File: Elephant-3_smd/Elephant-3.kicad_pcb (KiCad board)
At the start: 2 copper layers, 90.2 x 58.4 mm, 61 parts, among them CON1 ISP, J1 7-25V, J10 Micro_SD_Card, J11 IgnCap, J12 Main, J2 ADC2, J3 ADC1, J4 ADC0, J5 Switch, J6 18V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

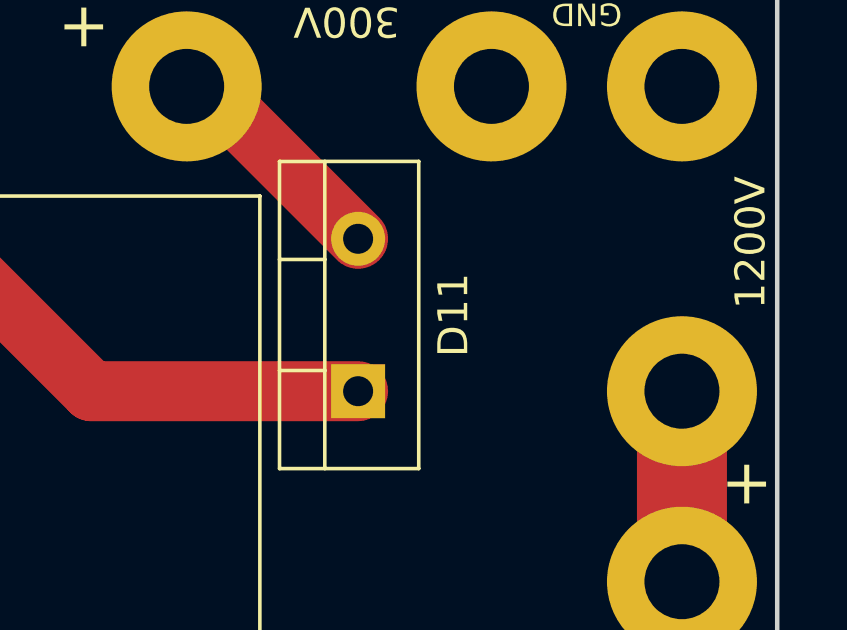
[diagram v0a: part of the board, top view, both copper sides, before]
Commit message: Added project files for smd version and replaced some component to generic
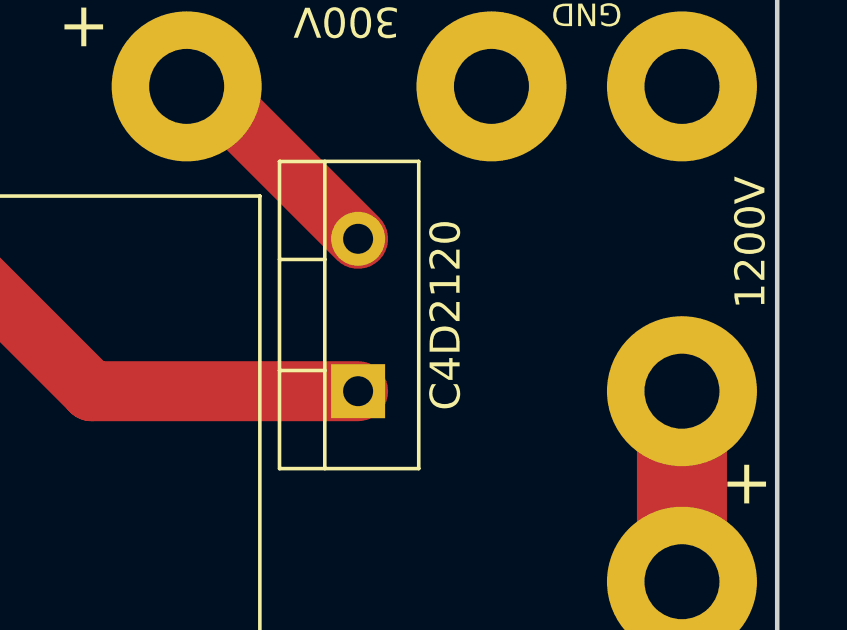
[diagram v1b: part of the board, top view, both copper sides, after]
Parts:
- D11: value D -> C4D2120
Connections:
- J10 pad 1: (no net) -> Net-(J10-Pad1)
- J10 pad 10: (no net) -> Net-(J10-Pad10)
- J10 pad 8: (no net) -> Net-(J10-Pad8)
- J10 pad 9: (no net) -> Net-(J10-Pad9)
- U2 pad 12: (no net) -> Net-(U2-Pad12)
- U2 pad 14: (no net) -> Net-(U2-Pad14)
- U2 pad 15: (no net) -> Net-(U2-Pad15)
- U2 pad 2: (no net) -> Net-(U2-Pad2)
- U2 pad 21: (no net) -> Net-(U2-Pad21)
- U2 pad 26: (no net) -> Net-(U2-Pad26)
- U2 pad 27: (no net) -> Net-(U2-Pad27)
- U2 pad 3: (no net) -> Net-(U2-Pad3)
- U2 pad 5: (no net) -> Net-(U2-Pad5)
- U2 pad 6: (no net) -> Net-(U2-Pad6)
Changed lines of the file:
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@@
     (zones 0)
     (modules 61)
-    (nets 35)
+    (nets 49)
   )
   (page A4)
@@
   (net 33 "Net-(C11-Pad1)")
   (net 34 "Net-(C13-Pad2)")
+  (net 35 "Net-(J10-Pad9)")
+  (net 36 "Net-(J10-Pad8)")
+  (net 37 "Net-(J10-Pad1)")
+  (net 38 "Net-(J10-Pad10)")
+  (net 39 "Net-(U2-Pad15)")
+  (net 40 "Net-(U2-Pad2)")
+  (net 41 "Net-(U2-Pad3)")
+  (net 42 "Net-(U2-Pad5)")
+  (net 43 "Net-(U2-Pad6)")
+  (net 44 "Net-(U2-Pad21)")
+  (net 45 "Net-(U2-Pad12)")
+  (net 46 "Net-(U2-Pad26)")
+  (net 47 "Net-(U2-Pad27)")
+  (net 48 "Net-(U2-Pad14)")
   (net_class Default "This is the default net class."
     (clearance 0.2)
@@
     (add_net "Net-(D4-Pad1)")
     (add_net "Net-(D6-Pad1)")
+    (add_net "Net-(J10-Pad1)")
+    (add_net "Net-(J10-Pad10)")
     (add_net "Net-(J10-Pad2)")
     (add_net "Net-(J10-Pad3)")
     (add_net "Net-(J10-Pad5)")
+    (add_net "Net-(J10-Pad8)")
+    (add_net "Net-(J10-Pad9)")
     (add_net "Net-(J5-Pad1)")
     (add_net "Net-(Q1-Pad1)")
     (add_net "Net-(Q2-Pad1)")
     (add_net "Net-(U2-Pad11)")
+    (add_net "Net-(U2-Pad12)")
     (add_net "Net-(U2-Pad13)")
+    (add_net "Net-(U2-Pad14)")
+    (add_net "Net-(U2-Pad15)")
     (add_net "Net-(U2-Pad16)")
+    (add_net "Net-(U2-Pad2)")
+    (add_net "Net-(U2-Pad21)")
+    (add_net "Net-(U2-Pad26)")
+    (add_net "Net-(U2-Pad27)")
+    (add_net "Net-(U2-Pad3)")
+    (add_net "Net-(U2-Pad5)")
+    (add_net "Net-(U2-Pad6)")
   )
   (net_class 1200V ""
@@
       (effects (font (size 1 1) (thickness 0.15)))
     )
-    (fp_text value D (at 2.54 -3.175 90) (layer F.Fab)
-      (effects (font (size 1 1) (thickness 0.15)))
-    )
-    (fp_text user %R (at 2.54 3.175 90) (layer F.SilkS)
+    (fp_text value C4D2120 (at 2.54 2.921 90) (layer F.SilkS)
+      (effects (font (size 1 1) (thickness 0.15)))
+    )
+    (fp_text user %R (at 2.54 -3.62 90) (layer F.Fab)
       (effects (font (size 1 1) (thickness 0.15)))
     )
@@
       (effects (font (size 0.6 0.6) (thickness 0.09)))
     )
-    (pad 9 smd rect (at -8.65 -0.6) (size 0.7 1.2) (layers F.Cu F.Paste F.Mask))
-    (pad 8 smd rect (at -7.7 -0.6) (size 0.7 1.2) (layers F.Cu F.Paste F.Mask))
-    (pad 1 smd rect (at 0 -0.6) (size 0.7 1.2) (layers F.Cu F.Paste F.Mask))
+    (pad 9 smd rect (at -8.65 -0.6) (size 0.7 1.2) (layers F.Cu F.Paste F.Mask)
+      (net 35 "Net-(J10-Pad9)"))
+    (pad 8 smd rect (at -7.7 -0.6) (size 0.7 1.2) (layers F.Cu F.Paste F.Mask)
+      (net 36 "Net-(J10-Pad8)"))
+    (pad 1 smd rect (at 0 -0.6) (size 0.7 1.2) (layers F.Cu F.Paste F.Mask)
+      (net 37 "Net-(J10-Pad1)"))
     (pad 2 smd rect (at -1.1 -0.6) (size 0.7 1.2) (layers F.Cu F.Paste F.Mask)
       (net 26 "Net-(J10-Pad2)"))
@@
     (pad 11 smd rect (at -9.6 3.7) (size 1 1.2) (layers F.Cu F.Paste F.Mask)
       (net 2 GND))
-    (pad 10 smd rect (at -9.6 9.9) (size 1 0.8) (layers F.Cu F.Paste F.Mask))
+    (pad 10 smd rect (at -9.6 9.9) (size 1 0.8) (layers F.Cu F.Paste F.Mask)
+      (net 38 "Net-(J10-Pad10)"))
     (pad 11 smd rect (at -9.6 14.05) (size 1 2.8) (layers F.Cu F.Paste F.Mask)
       (net 2 GND))
@@
     (pad 1 thru_hole rect (at 0 0) (size 2.4 1.6) (drill 0.8) (layers *.Cu *.Mask)
       (net 34 "Net-(C13-Pad2)"))
-    (pad 15 thru_hole oval (at 7.62 33.02) (size 2.4 1.6) (drill 0.8) (layers *.Cu *.Mask))
-    (pad 2 thru_hole oval (at 0 2.54) (size 2.4 1.6) (drill 0.8) (layers *.Cu *.Mask))
+    (pad 15 thru_hole oval (at 7.62 33.02) (size 2.4 1.6) (drill 0.8) (layers *.Cu *.Mask)
+      (net 39 "Net-(U2-Pad15)"))
+    (pad 2 thru_hole oval (at 0 2.54) (size 2.4 1.6) (drill 0.8) (layers *.Cu *.Mask)
+      (net 40 "Net-(U2-Pad2)"))
     (pad 16 thru_hole oval (at 7.62 30.48) (size 2.4 1.6) (drill 0.8) (layers *.Cu *.Mask)
       (net 32 "Net-(U2-Pad16)"))
-    (pad 3 thru_hole oval (at 0 5.08) (size 2.4 1.6) (drill 0.8) (layers *.Cu *.Mask))
+    (pad 3 thru_hole oval (at 0 5.08) (size 2.4 1.6) (drill 0.8) (layers *.Cu *.Mask)
+      (net 41 "Net-(U2-Pad3)"))
     (pad 17 thru_hole oval (at 7.62 27.94) (size 2.4 1.6) (drill 0.8) (layers *.Cu *.Mask)
       (net 11 "Net-(CON1-Pad4)"))
@@
     (pad 18 thru_hole oval (at 7.62 25.4) (size 2.4 1.6) (drill 0.8) (layers *.Cu *.Mask)
       (net 13 "Net-(CON1-Pad1)"))
-    (pad 5 thru_hole oval (at 0 10.16) (size 2.4 1.6) (drill 0.8) (layers *.Cu *.Mask))
+    (pad 5 thru_hole oval (at 0 10.16) (size 2.4 1.6) (drill 0.8) (layers *.Cu *.Mask)
+      (net 42 "Net-(U2-Pad5)"))
     (pad 19 thru_hole oval (at 7.62 22.86) (size 2.4 1.6) (drill 0.8) (layers *.Cu *.Mask)
       (net 12 "Net-(CON1-Pad3)"))
-    (pad 6 thru_hole oval (at 0 12.7) (size 2.4 1.6) (drill 0.8) (layers *.Cu *.Mask))
+    (pad 6 thru_hole oval (at 0 12.7) (size 2.4 1.6) (drill 0.8) (layers *.Cu *.Mask)
+      (net 43 "Net-(U2-Pad6)"))
     (pad 20 thru_hole oval (at 7.62 20.32) (size 2.4 1.6) (drill 0.8) (layers *.Cu *.Mask)
       (net 1 +5V))
     (pad 7 thru_hole oval (at 0 15.24) (size 2.4 1.6) (drill 0.8) (layers *.Cu *.Mask)
       (net 1 +5V))
-    (pad 21 thru_hole oval (at 7.62 17.78) (size 2.4 1.6) (drill 0.8) (layers *.Cu *.Mask))
+    (pad 21 thru_hole oval (at 7.62 17.78) (size 2.4 1.6) (drill 0.8) (layers *.Cu *.Mask)
+      (net 44 "Net-(U2-Pad21)"))
     (pad 8 thru_hole oval (at 0 17.78) (size 2.4 1.6) (drill 0.8) (layers *.Cu *.Mask)
       (net 2 GND))
@@
     (pad 25 thru_hole oval (at 7.62 7.62) (size 2.4 1.6) (drill 0.8) (layers *.Cu *.Mask)
       (net 5 "Net-(C6-Pad1)"))
-    (pad 12 thru_hole oval (at 0 27.94) (size 2.4 1.6) (drill 0.8) (layers *.Cu *.Mask))
-    (pad 26 thru_hole oval (at 7.62 5.08) (size 2.4 1.6) (drill 0.8) (layers *.Cu *.Mask))
+    (pad 12 thru_hole oval (at 0 27.94) (size 2.4 1.6) (drill 0.8) (layers *.Cu *.Mask)
+      (net 45 "Net-(U2-Pad12)"))
+    (pad 26 thru_hole oval (at 7.62 5.08) (size 2.4 1.6) (drill 0.8) (layers *.Cu *.Mask)
+      (net 46 "Net-(U2-Pad26)"))
     (pad 13 thru_hole oval (at 0 30.48) (size 2.4 1.6) (drill 0.8) (layers *.Cu *.Mask)
       (net 30 "Net-(U2-Pad13)"))
-    (pad 27 thru_hole oval (at 7.62 2.54) (size 2.4 1.6) (drill 0.8) (layers *.Cu *.Mask))
-    (pad 14 thru_hole oval (at 0 33.02) (size 2.4 1.6) (drill 0.8) (layers *.Cu *.Mask))
+    (pad 27 thru_hole oval (at 7.62 2.54) (size 2.4 1.6) (drill 0.8) (layers *.Cu *.Mask)
+      (net 47 "Net-(U2-Pad27)"))
+    (pad 14 thru_hole oval (at 0 33.02) (size 2.4 1.6) (drill 0.8) (layers *.Cu *.Mask)
+      (net 48 "Net-(U2-Pad14)"))
     (pad 28 thru_hole oval (at 7.62 0) (size 2.4 1.6) (drill 0.8) (layers *.Cu *.Mask)
       (net 4 "Net-(C4-Pad1)"))

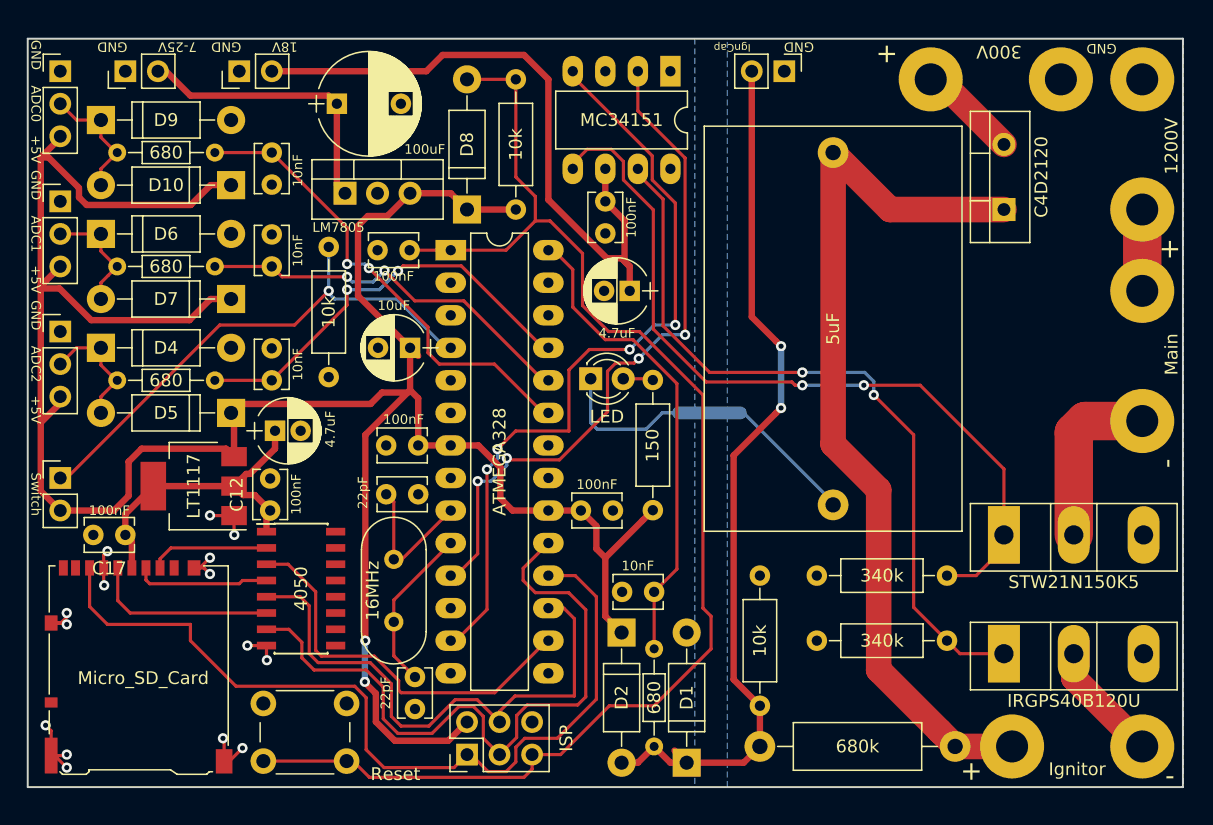
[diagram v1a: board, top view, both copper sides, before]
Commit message: routed everything except for ground
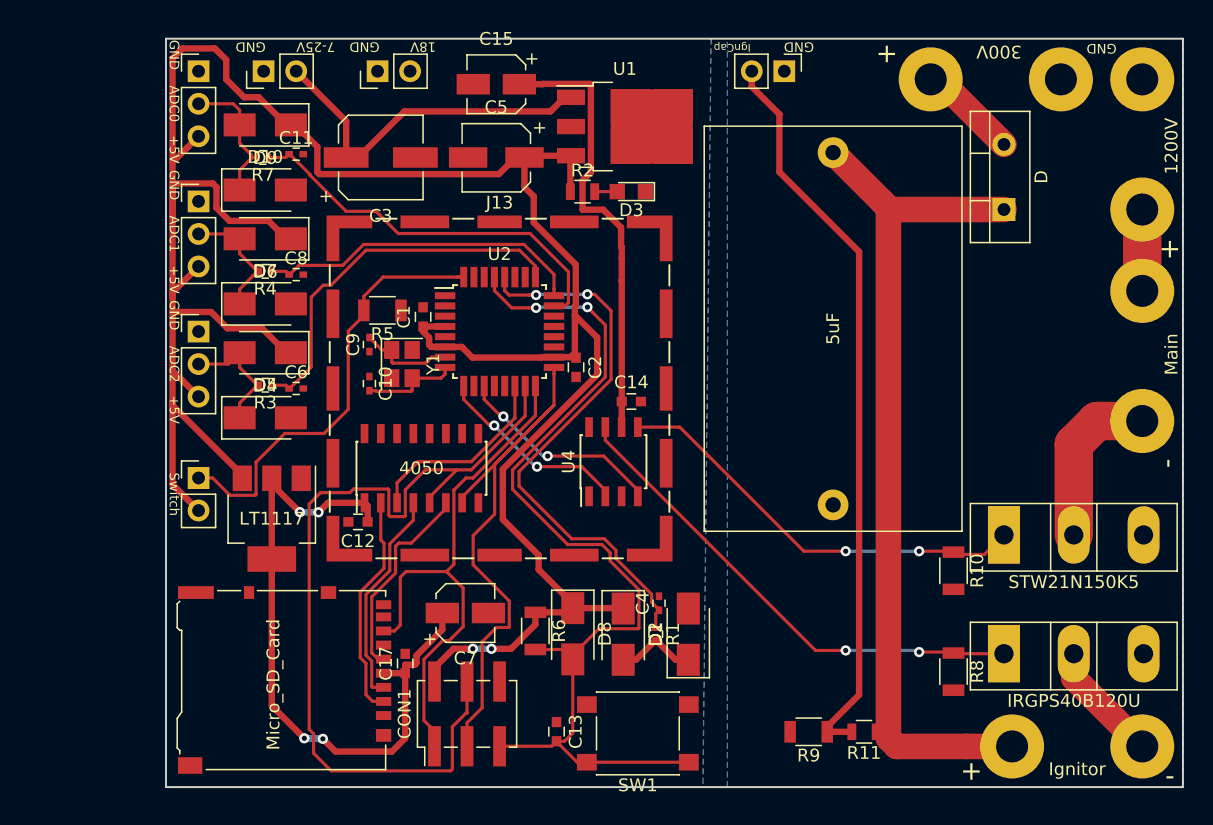
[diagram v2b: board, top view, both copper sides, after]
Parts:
- added J13: RF_Shield_Two_Pieces, Shielding_Cabinets:Laird_Technologies_BMI-S-203-F_26.21x26.21mm, F.Cu at (144.8, 95.9)
- C1, C12, C13, C14, C17, C2: footprint Capacitors_THT:C_Disc_D3.8mm_W2.6mm_P2.50mm -> Capacitors_SMD:C_0603
- C10, C11, C4, C6, C8, C9: footprint Capacitors_THT:C_Disc_D3.8mm_W2.6mm_P2.50mm -> Capacitors_SMD:C_0402
- C15, C7: footprint Capacitors_THT:CP_Radial_D5.0mm_P2.00mm -> Capacitors_SMD:CP_Elec_4x5.3
- C3: footprint Capacitors_THT:CP_Radial_D8.0mm_P5.00mm -> Capacitors_SMD:CP_Elec_6.3x5.3
- C5: footprint Capacitors_THT:CP_Radial_D5.0mm_P2.50mm -> Capacitors_SMD:CP_Elec_5x5.3
- CON1: footprint Pin_Headers:Pin_Header_Straight_2x03_Pitch2.54mm -> Pin_Headers:Pin_Header_Straight_2x03_Pitch2.54mm_SMD
- D1, D10, D2, D4, D5, D6, D7, D8, D9: footprint Diodes_THT:D_DO-41_SOD81_P10.16mm_Horizontal -> Diodes_SMD:D_SMA
- D11: value C4D2120 -> D
- D3: footprint LEDs:LED_D3.0mm -> LEDs:LED_0805
- R1, R3, R4, R7: footprint Resistors_THT:R_Axial_DIN0204_L3.6mm_D1.6mm_P7.62mm_Horizontal -> Resistors_SMD:R_0402
- R10, R5, R6, R8, R9: footprint Resistors_THT:R_Axial_DIN0207_L6.3mm_D2.5mm_P10.16mm_Horizontal -> Resistors_SMD:R_1206
- R11: footprint Resistors_THT:R_Axial_DIN0411_L9.9mm_D3.6mm_P15.24mm_Horizontal -> Resistors_SMD:R_0805
- R2: footprint Resistors_THT:R_Axial_DIN0207_L6.3mm_D2.5mm_P10.16mm_Horizontal -> Resistors_SMD:R_0805
- SW1: footprint Buttons_Switches_THT:SW_PUSH_6mm_h5mm -> Buttons_Switches_SMD:SW_SPST_PTS645
- U1: value LM7805 -> 7805; footprint TO_SOT_Packages_THT:TO-220-3_Vertical -> TO_SOT_Packages_SMD:TO-252-3_TabPin2
- U2: footprint Housings_DIP:DIP-28_W7.62mm_LongPads -> Housings_QFP:TQFP-32_7x7mm_Pitch0.8mm
- U4: footprint Housings_DIP:DIP-8_W7.62mm_LongPads -> Housings_SOIC:SOIC-8_3.9x4.9mm_Pitch1.27mm
- Y1: footprint Crystals:Crystal_HC49-4H_Vertical -> Crystals:Crystal_SMD_SeikoEpson_FA238-4pin_3.2x2.5mm
- moved C13 40.1 mm to (149.2, 122.7), turned to 270 degrees
- moved D8 34.1 mm to (150.5, 115.0), turned to 270 degrees
- moved R6 32.9 mm to (147.6, 114.8), turned to 270 degrees
- moved U4 30.8 mm to (153.7, 101.6), turned to 90 degrees
- moved C10 25.6 mm to (134.6, 95.5), turned to 270 degrees
- moved R2 25.5 mm to (151.3, 80.5), turned to 0 degrees
- moved C17 24.0 mm to (137.4, 117.3), turned to 90 degrees
- moved SW1 22.8 mm to (155.6, 122.8)
- moved U1 22.5 mm to (154.6, 75.4)
- moved C7 20.6 mm to (142.1, 113.4)
- moved C15 19.2 mm to (144.5, 72.1)
- moved J10 19.2 mm to (135.1, 121.4), turned to 270 degrees
- moved C5 16.3 mm to (144.5, 77.9)
- moved C14 15.8 mm to (155.1, 96.9), turned to 0 degrees
- moved Y1 15.3 mm to (137.2, 94.0)
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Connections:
- U2 pad 1: Net-(C13-Pad2) -> (no net)
- U2 pad 10: Net-(C10-Pad2) -> (no net)
- U2 pad 12: Net-(U2-Pad12) -> (no net)
- U2 pad 13: Net-(U2-Pad13) -> (no net)
- U2 pad 15: Net-(U2-Pad15) -> Net-(CON1-Pad4)
- U2 pad 16: Net-(U2-Pad16) -> Net-(CON1-Pad1)
- U2 pad 17: Net-(CON1-Pad4) -> Net-(CON1-Pad3)
- U2 pad 18: Net-(CON1-Pad1) -> +5V
- U2 pad 19: Net-(CON1-Pad3) -> (no net)
- U2 pad 2: Net-(U2-Pad2) -> (no net)
- U2 pad 20: +5V -> (no net)
- U2 pad 21: Net-(U2-Pad21) -> GND
- U2 pad 22: GND -> (no net)
- U2 pad 26: Net-(U2-Pad26) -> (no net)
- U2 pad 27: Net-(U2-Pad27) -> (no net)
- U2 pad 3: Net-(U2-Pad3) -> GND
- U2 pad 4: Net-(J5-Pad1) -> +5V
- U2 pad 5: Net-(U2-Pad5) -> GND
- U2 pad 6: Net-(U2-Pad6) -> +5V
- U2 pad 7: +5V -> Net-(C9-Pad2)
- U2 pad 8: GND -> Net-(C10-Pad2)
- U2 pad 9: Net-(C9-Pad2) -> Net-(U2-Pad9)
- U4 pad 2: Net-(U2-Pad11) -> Net-(U2-Pad9)
- U4 pad 4: Net-(U2-Pad13) -> Net-(U2-Pad11)
- U5 pad 3: Net-(U2-Pad16) -> Net-(U2-Pad14)
- Y1 pad 2: Net-(C10-Pad2) -> GND
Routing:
- net Net-(U2-Pad13): track 60.5 -> 0.00 mm, vias 4 -> 0
- net GND: track 50.1 -> 0.00 mm, vias 15 -> 0
- net Net-(U2-Pad11): track 53.8 -> 16.5 mm, vias 4 -> 2
- net Net-(C13-Pad2): track 107.7 -> 75.7 mm, vias 0 -> 2
- net Net-(U2-Pad16): track 31.0 -> 0.00 mm
- net Net-(Q2-Pad1): track 62.6 -> 32.9 mm
- net +3V3: track 26.6 -> 55.2 mm, vias 0 -> 4
- net Net-(CON1-Pad1): track 67.3 -> 41.6 mm
- net Net-(CON1-Pad4): track 43.8 -> 67.4 mm
- net Net-(Q1-Pad1): track 58.8 -> 38.7 mm
- net 18V: track 51.1 -> 34.8 mm
- net Net-(U2-Pad9): track 0.00 -> 15.5 mm, vias 0 -> 2
- net Net-(U2-Pad14): track 0.00 -> 15.4 mm
- net Net-(J10-Pad2): track 9.37 -> 18.1 mm
- net +5V: track 207.7 -> 200.0 mm
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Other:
- board size 90.2 x 58.4 mm -> 79.4 x 58.4 mm
- net class 300V-signal: clearance 1 -> 0.4
- rule pad_to_mask_clearance: 0.2 -> 0

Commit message: Added missing tracks
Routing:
- net IgnCap: track 64.3 -> 77.4 mm
- net 18V: track 34.8 -> 44.0 mm
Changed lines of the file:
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@@
     (thickness 1.6)
     (drawings 19)
-    (tracks 467)
+    (tracks 474)
     (zones 0)
     (modules 62)
@@
   (segment (start 142.71059 102.87) (end 147.58 98.00059) (width 0.25) (layer F.Cu) (net 13))
   (segment (start 147.58 98.00059) (end 147.58 95.69) (width 0.25) (layer F.Cu) (net 13) (status 20))
-  (segment (start 170.36 122.682) (end 170.36 122.282) (width 0.5) (layer F.Cu) (net 14))
+  (segment (start 159.512 117.062) (end 165.14 117.062) (width 0.5) (layer F.Cu) (net 14))
+  (segment (start 165.14 117.062) (end 170.36 122.282) (width 0.5) (layer F.Cu) (net 14))
+  (segment (start 170.36 122.282) (end 170.36 122.682) (width 0.5) (layer F.Cu) (net 14))
   (segment (start 166.624 78.994) (end 166.624 74.481081) (width 0.5) (layer F.Cu) (net 14))
   (segment (start 166.624 74.481081) (end 164.465 72.322081) (width 0.5) (layer F.Cu) (net 14))
@@
   (segment (start 141.455 87.19) (end 141.98 87.19) (width 0.25) (layer F.Cu) (net 20) (status 20))
   (segment (start 141.98 86.665) (end 141.98 87.19) (width 0.25) (layer F.Cu) (net 20) (status 30))
+  (segment (start 137.795 71.12) (end 138.997081 71.12) (width 0.5) (layer F.Cu) (net 21))
+  (segment (start 138.997081 71.12) (end 139.281081 70.836) (width 0.5) (layer F.Cu) (net 21))
+  (segment (start 139.281081 70.836) (end 144.526 70.836) (width 0.5) (layer F.Cu) (net 21))
+  (segment (start 145.826 72.136) (end 146.326 72.136) (width 0.5) (layer F.Cu) (net 21))
+  (segment (start 144.526 70.836) (end 145.826 72.136) (width 0.5) (layer F.Cu) (net 21))
   (segment (start 154.317 96.901) (end 154.317 98.888) (width 0.5) (layer F.Cu) (net 21))
   (segment (start 154.317 98.888) (end 154.305 98.9) (width 0.5) (layer F.Cu) (net 21))

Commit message: Finished routing ground
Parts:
- U1: footprint TO_SOT_Packages_SMD:TO-252-3_TabPin2 -> TO_SOT_Packages_SMD:TO-252-2
- moved R5 1.57 mm to (135.3, 88.3), turned to 90 degrees
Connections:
- J10 pad 1: Net-(J10-Pad1) -> (no net)
- J10 pad 10: Net-(J10-Pad10) -> (no net)
- J10 pad 8: Net-(J10-Pad8) -> (no net)
- J10 pad 9: Net-(J10-Pad9) -> (no net)
- U2 pad 1: (no net) -> Net-(U2-Pad1)
- U2 pad 10: (no net) -> Net-(U2-Pad10)
- U2 pad 12: (no net) -> Net-(U2-Pad12)
- U2 pad 13: (no net) -> Net-(U2-Pad13)
- U2 pad 19: (no net) -> Net-(U2-Pad19)
- U2 pad 2: (no net) -> Net-(U2-Pad2)
- U2 pad 20: (no net) -> Net-(U2-Pad20)
- U2 pad 22: (no net) -> Net-(U2-Pad22)
- U2 pad 26: (no net) -> Net-(U2-Pad26)
- U2 pad 27: (no net) -> Net-(U2-Pad27)
- U2 pad 30: (no net) -> Net-(U2-Pad30)
- U2 pad 31: (no net) -> Net-(U2-Pad31)
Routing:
- net GND: track 0.00 -> 214.1 mm, vias 0 -> 94
- net Net-(C11-Pad1): track 31.0 -> 36.6 mm
- net Net-(CON1-Pad1): track 41.6 -> 44.2 mm
- net Net-(Q2-Pad1): track 32.9 -> 35.3 mm
- net 300V: track 66.5 -> 68.8 mm
- net Net-(J5-Pad1): track 35.3 -> 36.9 mm
- net Net-(Q1-Pad1): track 38.7 -> 39.7 mm
- net Net-(C6-Pad1): track 29.8 -> 30.4 mm
- net Net-(J10-Pad5): track 15.8 -> 16.4 mm
- net Net-(J10-Pad3): track 17.0 -> 17.6 mm
- added copper zone on F.Cu, net +3V3
- added copper zone on F.Cu, net GND
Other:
- net class GND added: clearance 0.2, trace_width 0.5, via_dia 0.8, via_drill 0.4

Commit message: Finished Labes
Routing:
- net GND: track 214.1 -> 222.1 mm, vias 94 -> 100

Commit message: Added name/version on to pcb
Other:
- board text added: "Designed by Corwin Hansen UW APL Ver. 1.0"
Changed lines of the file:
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@@
   (general
     (thickness 1.6)
-    (drawings 19)
+    (drawings 20)
     (tracks 781)
     (zones 0)
@@
     )
   )
+  (gr_text "Designed by Corwin Hansen   UW APL  Ver. 1.0\n" (at 157.48 85.09) (layer B.SilkS)
+    (effects (font (size 1.5 1.5) (thickness 0.3)) (justify mirror))
+  )
   (gr_line (start 118.745 127) (end 198.12 127) (angle 90) (layer Edge.Cuts) (width 0.15))
